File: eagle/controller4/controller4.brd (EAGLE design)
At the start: 50.5 x 64.8 mm, 62 parts, among them Q1 check_pins, Q3 check_pins, X1 1501_04

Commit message: controller4: eagle files nearly finished
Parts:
- removed H3: MOUNT-HOLE2.8, holes:2,8
- removed J4: (no value), SparkFun-Connectors:2X8
- removed JP1: JUMPER-PAD-2-NOYES_SILK, SparkFun-Passives:PAD-JUMPER-2-NO_YES_SILK
- removed U$1: USB-CON-5PIN-105017-0001, GeekAmmo:USB-MICRO-MOLEX-105017-0001
- added D1: 1N4004, adafruit:DO41-10
- added D2: (no value), SparkFun-LED:WS2812B
- added J1: (no value), SparkFun-Connectors:1X02_LOCK_LONGPADS
- added J3: (no value), SparkFun-Connectors:2X10
- added JP2: (no value), SparkFun-Passives:PAD-JUMPER-2-NO_YES_SILK
- added R2: (no value), SparkFun-Resistors:1206
- added RTC1: DS3231M, SparkFun-DigitalIC:SOIC8
- added R_LED: UNKNOWN, SparkFun-Resistors:1206
- added SH1: SHORT-HT5, shorts-old:SHORT_TOP-50
- added TP1: TPB1,27, testpad:B1,27
- added T_ZERO_N: (no value), SparkFun-DiscreteSemi:TO-92
- added X2: ZX62D-B-5PA8, zx62d-b-5pa8-oshpark_10:ZX62D-B-5PA8
- C4, C5: value (none) -> 22pF
- moved H4 82.8 mm to (20.3, 54.6)
- moved H2 58.8 mm to (20.3, 0.00)
- moved T_HSS 26.7 mm to (34.3, 16.5), turned to 0 degrees
- moved Q2 21.6 mm to (39.4, 25.4)
- moved R17 21.6 mm to (39.4, 17.8)
- moved RB1 18.9 mm to (39.4, 35.6)
- moved S1 18.0 mm to (40.6, 43.2)
- moved CONV_X_VCC 18.0 mm to (48.3, 36.8)
- moved J6 16.7 mm to (49.5, 26.7)
- moved J5 15.5 mm to (49.5, 19.1)
- moved RB5 15.3 mm to (38.1, 33.0), turned to 0 degrees
- moved RB2 14.2 mm to (31.8, 48.3), turned to 180 degrees
- moved R18 13.9 mm to (33.8, 23.4), turned to 270 degrees
- moved RB3 12.0 mm to (31.8, 44.5), turned to 180 degrees
- moved RB4 12.0 mm to (31.8, 40.6), turned to 180 degrees
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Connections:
- removed net FOO: U$3.32
- new net LED: R_LED.1, U$3.32
- new net N$10: RUSB1.2, X2.2
- new net N$13: J3.12, JP2.1
- new net N$16: D1.A, Q2.3
- new net N$18: R10.2, T_ZERO_N.3
- new net VBAT: J1.1, RTC1.6
- net +5V: now also J3.1, J3.3; no longer J4.1, J4.3
- net BTN_C: now also U$3.41; no longer U$3.39
- net BTN_D: now also U$3.37; no longer U$3.36
- net BTN_L: now also U$3.40; no longer U$3.38
- net BTN_R: now also U$3.38; no longer U$3.37
- net BTN_U: now also U$3.39; no longer U$3.40
- net CAM_EN: now also U$3.36; no longer U$3.41
- net CAM_OUT: now also D1.C; no longer Q2.3
- net CELL1: now also U$3.28; no longer U$3.29
- net CELL2: now also U$3.27; no longer U$3.28
- net GND: now also D2.3, J1.2, J3.5, RTC1.5, SH1.1, TP1.TP, T_ZERO_N.1, X2.5; no longer J4.5, U$1.5
- net GNDA: now also SH1.2
- net N$11: now also RUSB2.2, X2.3; no longer RUSB1.2, U$1.2
- net N$14: now also R2.1, T_ZERO_N.2; no longer RUSB2.2, U$1.3
- net N$22: now also X2.1; no longer U$1.1
- net N$7: now also D2.4, R_LED.2; no longer J4.12, JP1.1
- net RST: now also JP2.2; no longer JP1.2
- net SCL: now also RTC1.8
- net SDA: now also RTC1.7
- net VCC: now also D2.1, RTC1.2
- net VD_DIRECT: now also U$3.29; no longer U$3.27
- net ZERO_EN: now also R2.2; no longer R10.2
- net ZRX: now also J3.9; no longer J4.9
- net ZTX: now also J3.7; no longer J4.7
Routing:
- net GND: track 0.00 -> 344.3 mm, vias 0 -> 3
- net VCC: track 0.00 -> 226.3 mm, vias 0 -> 4
- net N$22: track 0.00 -> 63.8 mm, vias 0 -> 2
- net RX: track 0.00 -> 39.6 mm, vias 0 -> 1
- net CONV_5V: track 0.00 -> 38.8 mm
- net BATT_VCC: track 0.00 -> 36.0 mm
- net CELL2: track 0.00 -> 32.6 mm
- net VD_DIRECT: track 0.00 -> 32.5 mm
- net BTN_U: track 0.00 -> 31.7 mm
- net SCL: track 0.00 -> 28.7 mm, vias 0 -> 1
- net SDA: track 0.00 -> 27.7 mm, vias 0 -> 1
- net RST: track 0.00 -> 26.3 mm, vias 0 -> 1
- net BTN_R: track 0.00 -> 25.2 mm
- net BTN_C: track 0.00 -> 24.1 mm
- net MOSI: track 0.00 -> 23.7 mm, vias 0 -> 1
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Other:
- board size 50.5 x 64.8 mm -> 53 x 64.8 mm

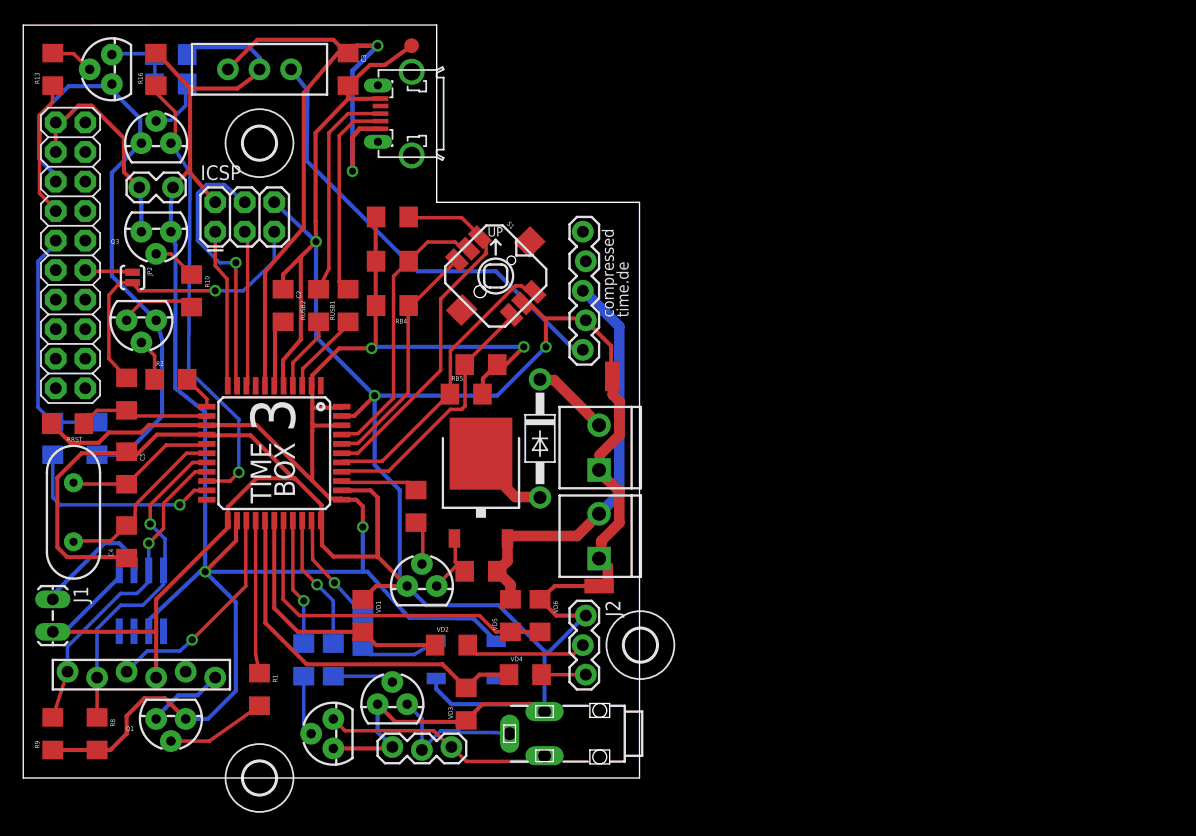
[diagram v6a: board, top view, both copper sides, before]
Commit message: controller4: fixed remaining airwires
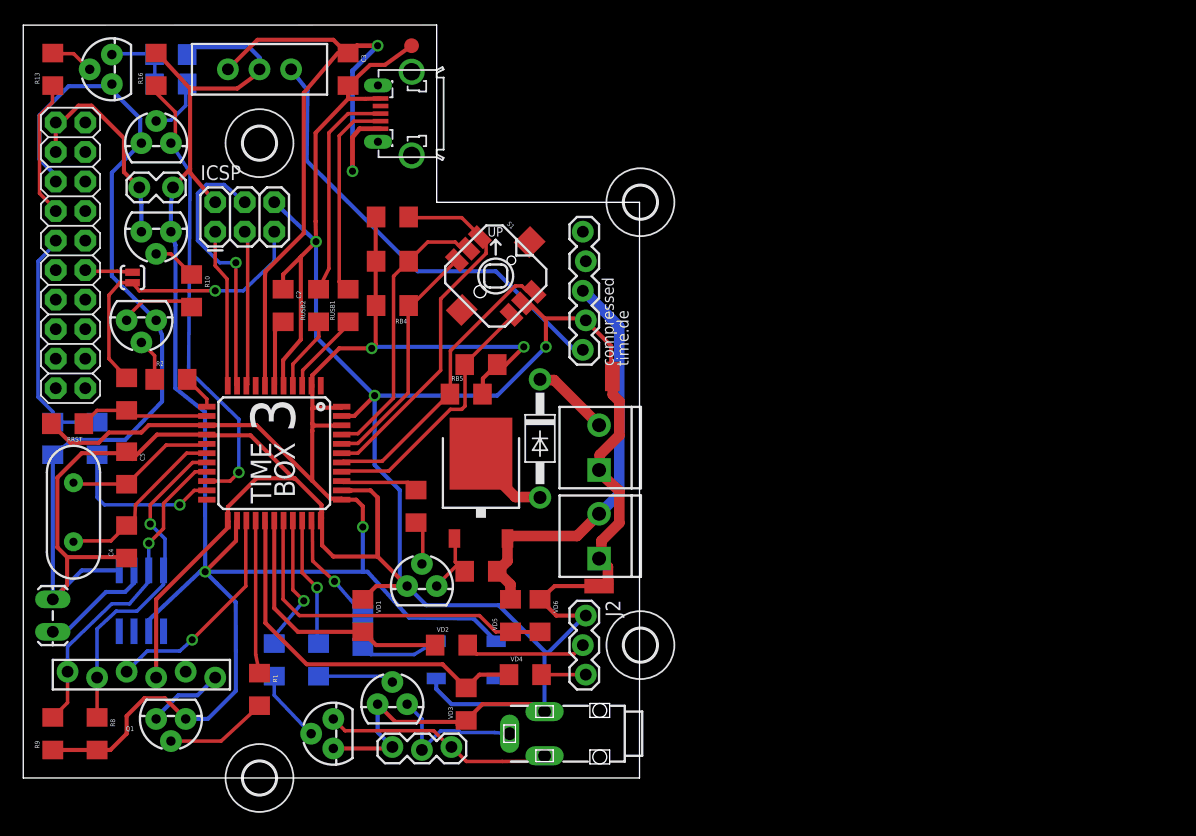
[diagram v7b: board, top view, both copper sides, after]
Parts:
- added H3: MOUNT-HOLE2.8, holes:2,8
- Q3: value check_pins -> (none)
- R16: value high ohm value -> 10k
- R20, R21: value (none) -> 1k
- R_LED: value UNKNOWN -> 4.7k
- moved R11 3.81 mm to (2.54, 29.2)
- moved R12 3.81 mm to (6.35, 29.2)
- moved J1 2.54 mm to (2.54, 12.7), turned to 90 degrees
- moved R21 2.54 mm to (21.6, 10.2)
- moved R20 1.27 mm to (25.4, 10.2)
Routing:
- net GND: track 344.3 -> 352.3 mm
- net TX: track 17.7 -> 13.9 mm
- net N$35: track 5.29 -> 6.56 mm
- net VBAT: track 10.9 -> 9.81 mm
- net N$32: track 5.21 -> 6.23 mm
- net CAM1: track 11.0 -> 11.9 mm
- net CAM2: track 11.7 -> 11.1 mm

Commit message: controller4: temp sensor and silkscreen
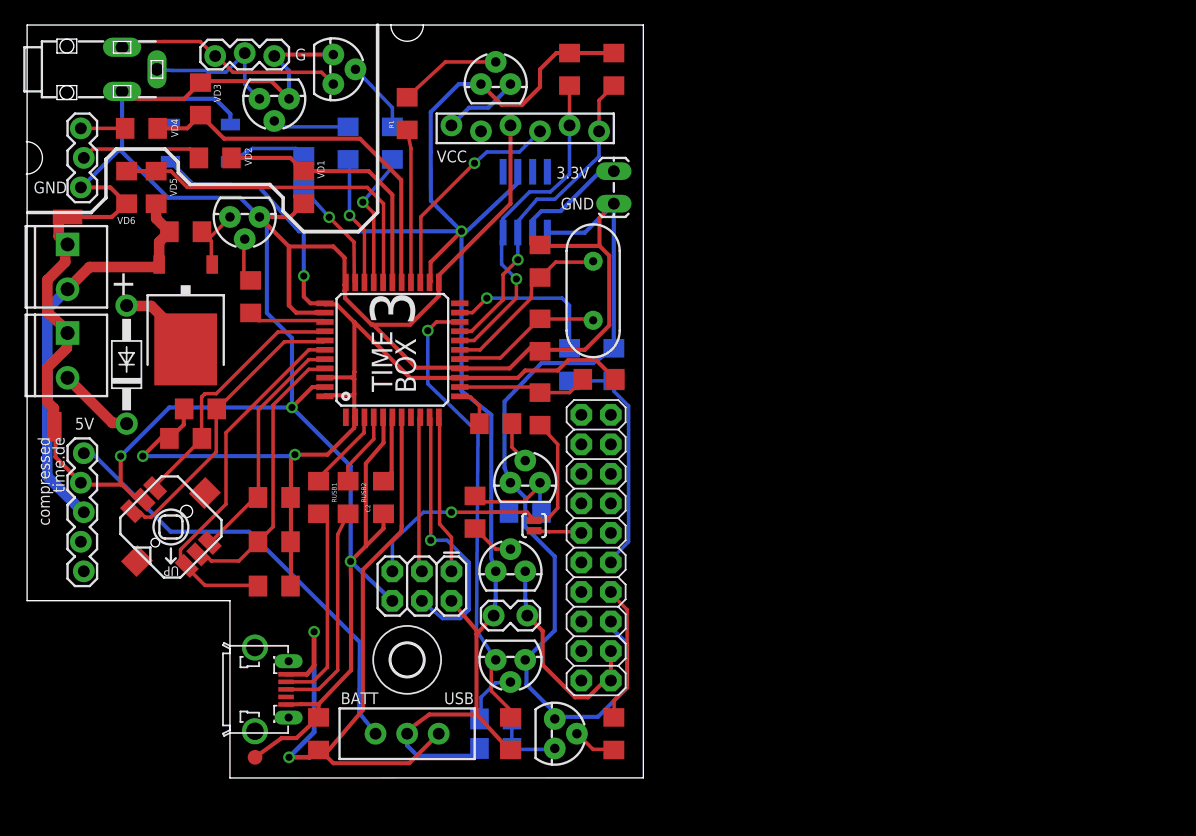
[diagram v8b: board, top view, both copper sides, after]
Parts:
- removed H1, H2, H3: MOUNT-HOLE2.8, holes:2,8
- added R3: (no value), SparkFun-Resistors:1206
- Q1: value check_pins -> (none)
- moved X1 78.2 mm to (0.00, 61.0), turned to 90 degrees
- moved R13 74.8 mm to (50.8, 3.81), turned to 270 degrees
- moved R9 74.8 mm to (50.8, 61.0), turned to 270 degrees
- moved R8 70.1 mm to (47.0, 61.0), turned to 90 degrees
- moved T_SHIFTER1 68.7 mm to (45.7, 3.81), turned to 270 degrees
- moved R15 65.9 mm to (40.6, 2.54), turned to 0 degrees
- moved DISP 65.6 mm to (49.5, 55.9), turned to 180 degrees
- moved R16 64.8 mm to (41.9, 3.81), turned to 270 degrees
- moved TP1 62.7 mm to (19.9, 1.78), turned to 180 degrees
- moved J1 62.3 mm to (50.8, 52.1), turned to 270 degrees
- moved Q1 61.3 mm to (40.6, 59.7), turned to 0 degrees
- moved R14 61.3 mm to (40.6, 5.08), turned to 0 degrees
- moved SHTR 60.5 mm to (21.6, 62.2), turned to 180 degrees
- moved S2 58.5 mm to (33.0, 3.81), turned to 90 degrees
- moved VD4 57.4 mm to (10.2, 55.9), turned to 180 degrees
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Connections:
- net N$18: now also R3.2
- net VCC: now also R3.1
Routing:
- net N$18: track 6.63 -> 9.30 mm
- net VCC: track 226.3 -> 227.8 mm
- net ZERO_EN: track 3.05 -> 3.56 mm
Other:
- board size 53 x 64.8 mm -> 53.1 x 64.8 mm
- board text added: "+"
- board text added: "-"
- board text added: "3.3V"
- board text added: "5V"
- board text added: "BATT"
- board text added: "G"
- board text added: "GND"
- board text added: "USB"
- board text added: "VCC"
